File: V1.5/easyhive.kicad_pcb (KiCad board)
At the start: 2 copper layers, 35 x 75 mm, 104 parts, among them IC1 ATSAMD21G, IC2 BQ2407X, IC3 ADS1232, IC4 DS18B20U, IC5 XC6220B331, IC6 SARA-N310, IC7 TPS22919, J1 U.FL, J2 U.FL(2), K1 693043020611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

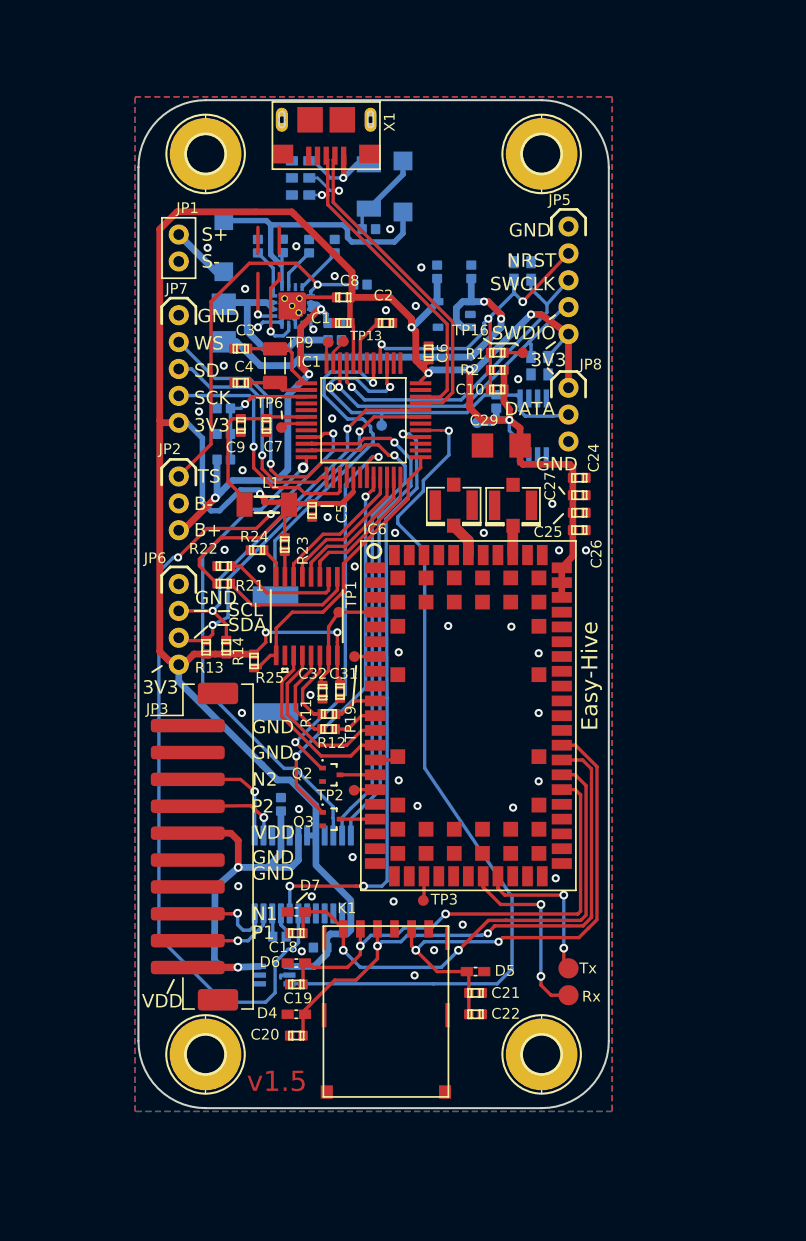
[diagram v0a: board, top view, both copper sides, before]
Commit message: v1.5 Oertel with optimizations
-fixed problems/questions from Oertel
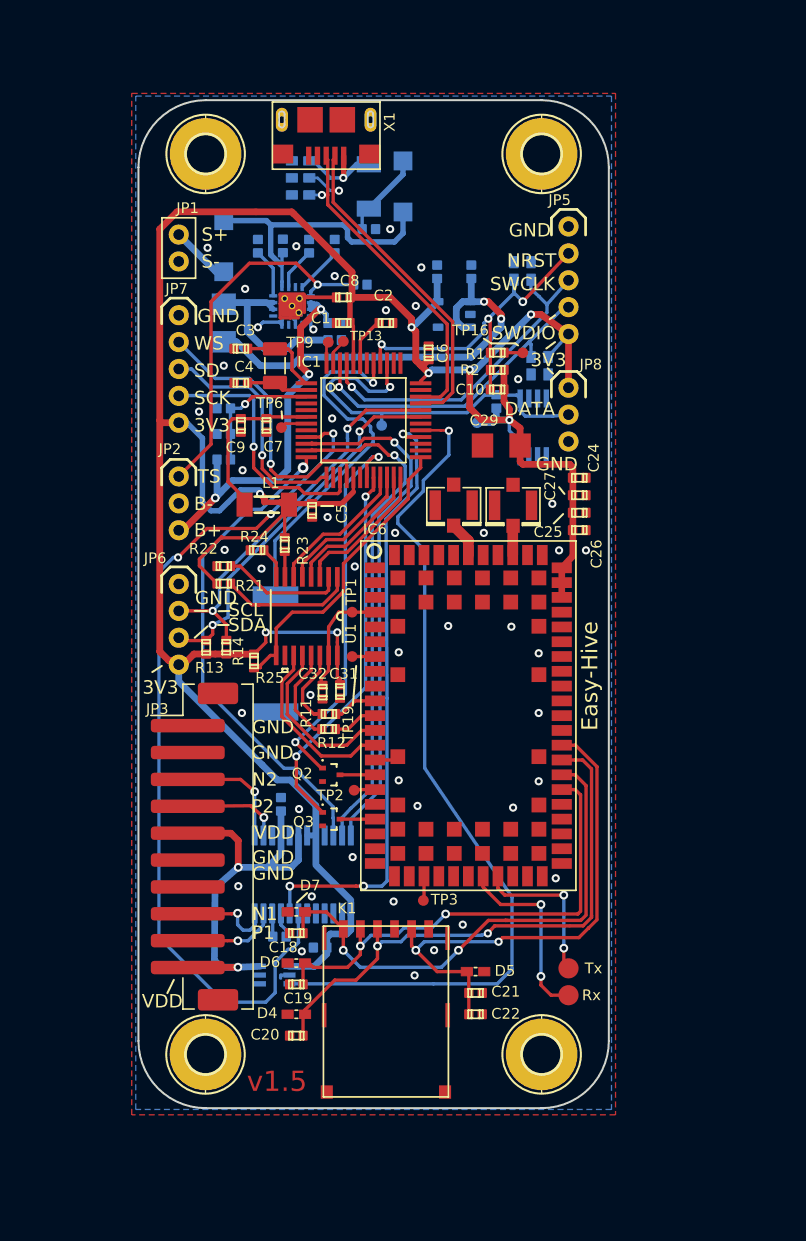
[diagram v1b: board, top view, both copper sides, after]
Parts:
- D1, D2: footprint easyhive:SOD123 -> easyhive:SOD-123
- L1, L2: value SM-1206 -> (none)
- moved TP1 1.00 mm to (146.9, 105.6)
- moved TP19 0.17 mm to (146.9, 108.9)
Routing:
- net Net-(IC2-Pad7): track 6.66 -> 0.00 mm, vias 1 -> 0
- net Net-(IC2-Pad9): track 4.25 -> 0.00 mm, vias 1 -> 0
- net Net-(LED2-PadA): track 1.92 -> 0.00 mm
- net Net-(LED1-PadA): track 1.92 -> 0.00 mm

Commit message: Begin Routing
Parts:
- removed IC6: SARA-N310, easyhive:SARA-N3
- removed J2: U.FL(2), easyhive:U.FL
- removed R11, R12, R21: 0R, easyhive:C0402
- removed TP1, TP19, TP2, TP3: TPTP08R, easyhive:TP08R
- added D15: PESD0402-140, easyhive:0402-TVS, F.Cu at (153.2, 102.3)
- added JP10: USB_BC66, easyhive:1X04-2MM_klein, F.Cu at (163.0, 127.8)
- added JP9: DBG, easyhive:1X02_2MM_klein, F.Cu at (163.0, 96.0)
- added Q4: DTC123JET1G, easyhive:SC75_SOT416, F.Cu at (156.4, 125.8)
- added R6: 10K, easyhive:C0402, F.Cu at (141.9, 122.7)
- added R7: 22R, easyhive:C0402, F.Cu at (144.5, 123.8)
- added R8: 22R, easyhive:C0402, F.Cu at (143.2, 123.8)
- added R9: 22R, easyhive:C0402, F.Cu at (145.8, 124.2)
- added U2: BC66, easyhive:Quectel_BC66, F.Cu at (155.2, 113.8)
- C22: value 100n -> 100nF
- D1, D2: footprint easyhive:SOD-123 -> easyhive:SOD123
- JP4: value M02-JST-2MM-SMT -> AUX; footprint easyhive:1X02_2MM_Pad_only -> easyhive:1X02_2MM_klein
- L1, L2: value (none) -> SM-1206
- moved C24 10.8 mm to (153.1, 97.0)
- moved C26 10.8 mm to (153.1, 100.9)
- moved C25 10.8 mm to (153.1, 99.6)
- moved C27 10.8 mm to (153.1, 98.3)
- moved JP4 9.10 mm to (163.0, 123.0)
- moved Q3 8.17 mm to (152.0, 125.8)
- moved J1 6.78 mm to (163.0, 103.0)
- moved C22 4.52 mm to (156.0, 131.0), turned to 270 degrees
- moved C31 2.12 mm to (144.5, 113.0)
- moved U1 2.12 mm to (142.5, 107.8)
- moved C32 2.05 mm to (143.2, 113.0)
- moved R23 1.88 mm to (140.8, 102.1)
- moved Q2 1.70 mm to (143.8, 116.9)
- moved C29 1.39 mm to (157.3, 94.4), turned to 0 degrees
- moved R25 1.30 mm to (138.8, 108.2), turned to 0 degrees
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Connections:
- net /SARA_1V8_ENABLE renamed /BC66_1V8_ENABLE
- net /SARA_CTS_3V3 renamed /BC66_RI_3V3
- net /SARA_PWRON renamed /BC66_PWRON
- net /SARA_RST renamed /BC66_RST
- net /SARA_RX_3V3 renamed /BC66_RXD_3V3
- net /SARA_TX_3V3 renamed /BC66_TXD_3V3
- C22 pad 1: Net-(C21-Pad1) -> GND
- C22 pad 2: GND -> Net-(C21-Pad1)
- IC1 pad 24: /SARA_RTS_3V3 -> Net-(IC1-Pad24)
- IC1 pad 8: Net-(IC1-Pad8) -> /BC66_PSM
- J1 pad P$3: /ANT -> Net-(J1-PadP$3)
- R23 pad 1: +3V3 -> GND
- R24 pad 1: GND -> +3V3
- U1 pad 11: /SARA_RX_1V8 -> /BC66_RXD_1V8
- U1 pad 12: /SARA_TX_1V8 -> /BC66_TXD_1V8
- U1 pad 13: /CTS1V8 -> /BC66_RI_1V8
- U1 pad 14: /RTS1V8 -> Net-(U1-Pad14)
- U1 pad 3: /SARA_RTS_3V3 -> Net-(U1-Pad3)
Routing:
- net Net-(C18-Pad1): track 38.8 -> 5.02 mm, vias 2 -> 0
- net Net-(C21-Pad1): track 38.5 -> 9.19 mm, vias 2 -> 0
- net Net-(C20-Pad1): track 41.6 -> 13.7 mm, vias 2 -> 1
- net Net-(C19-Pad1): track 35.9 -> 15.5 mm
- net +3V3: track 213.0 -> 194.5 mm, vias 8 -> 6
- net Net-(JP4-Pad2): track 14.0 -> 0.00 mm, vias 2 -> 0
- net /SARA_RX_1V8: track 13.4 -> 0.00 mm
- net /SARA_TX_1V8: track 12.8 -> 0.00 mm
- net /BC66_RST: track 28.5 -> 16.0 mm, vias 2 -> 1
- net Net-(JP9-Pad1): track 0.00 -> 12.0 mm
- net Net-(JP4-Pad1): track 11.6 -> 0.00 mm, vias 2 -> 0
- net /SARA_RTS_3V3: track 10.7 -> 0.00 mm
- net Net-(U1-Pad1): track 10.4 -> 0.00 mm
- net Net-(JP9-Pad2): track 0.00 -> 9.55 mm
- net /+1V8: track 8.65 -> 0.00 mm
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- removed copper zone on B.Cu, net GND
- removed copper zone on F.Cu, net GND

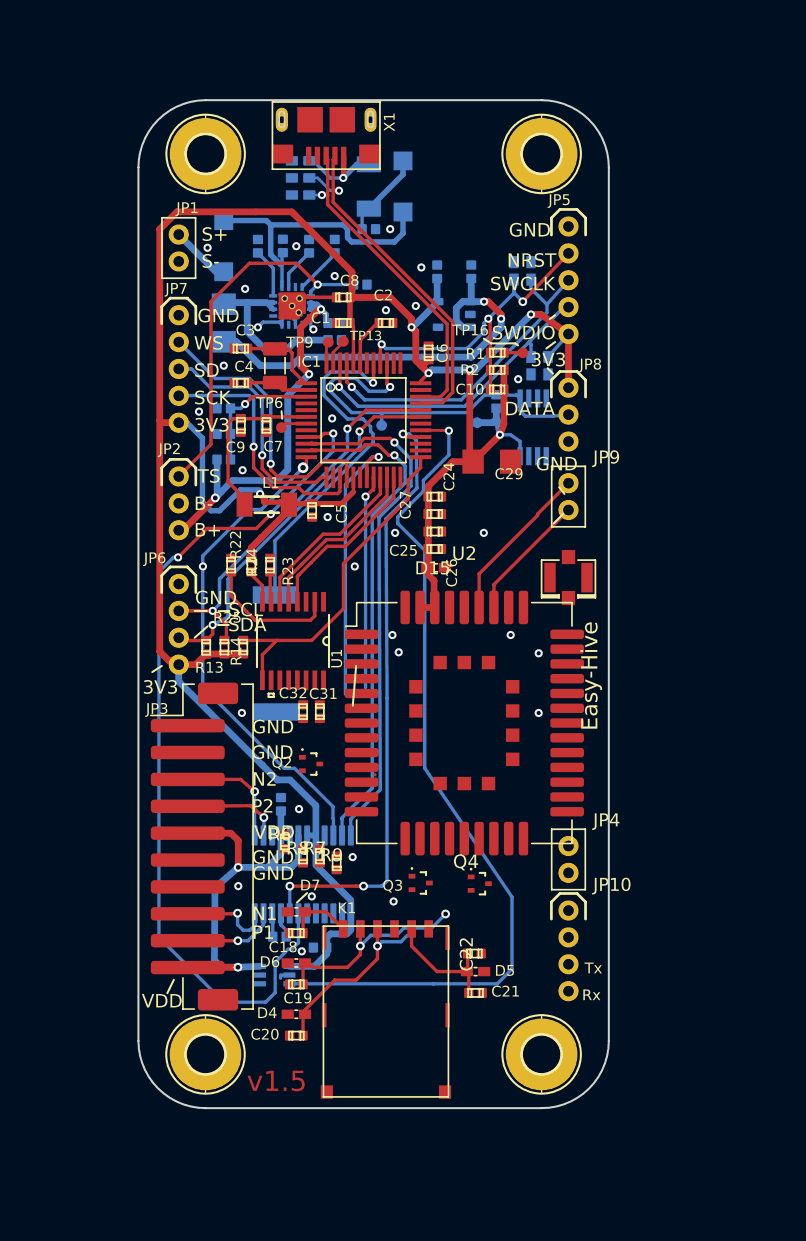
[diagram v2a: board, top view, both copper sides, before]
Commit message: try to route...
DRC Checker meckert wegen Bauteilüberschneidung. BC66 hat im Footprint mega Rahmen... Laut Description ist es 17,7mm breit, der Rahmen hat aber über 20mm...
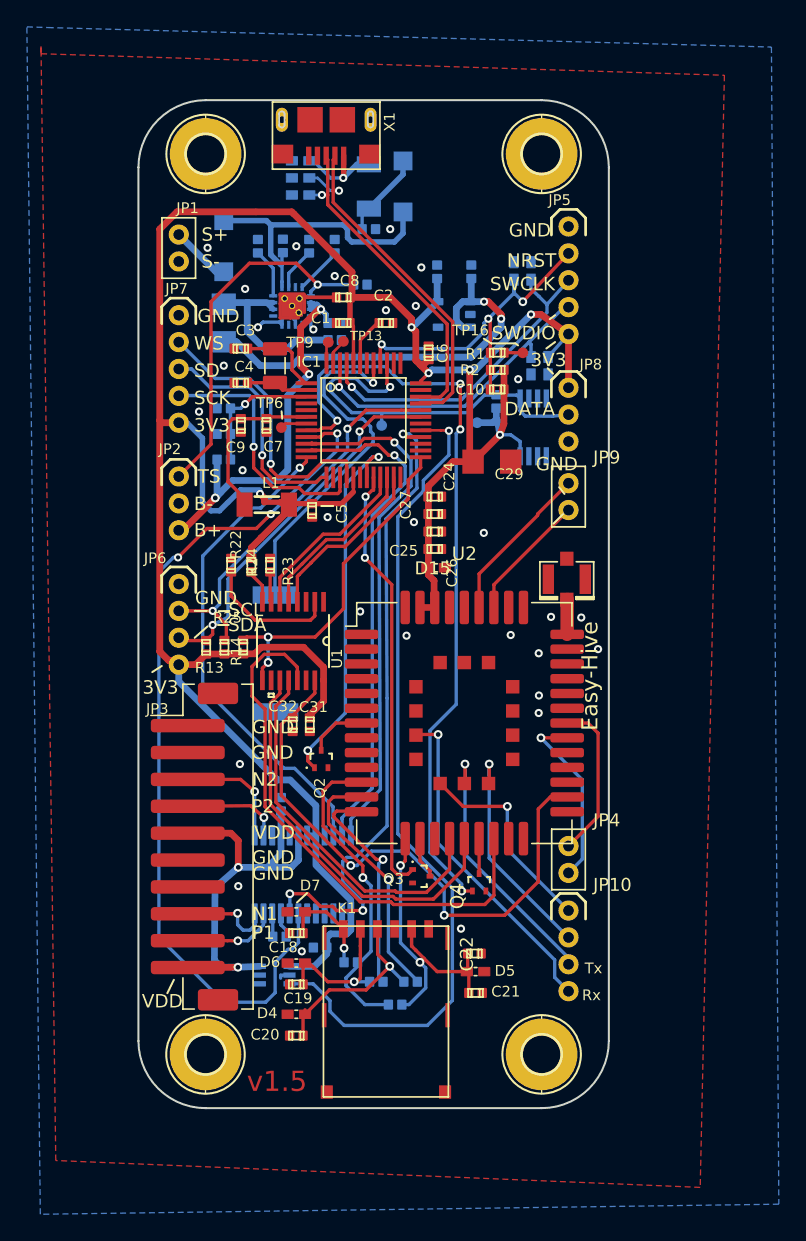
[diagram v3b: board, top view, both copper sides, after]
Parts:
- R6, R7, R8, R9: moved to B.Cu
- moved R6 14.6 mm to (150.1, 134.8), turned to 90 degrees
- moved R7 11.5 mm to (151.2, 133.1), turned to 90 degrees
- moved R9 9.33 mm to (148.7, 133.1), turned to 90 degrees
- moved R8 8.66 mm to (146.8, 131.7), turned to 90 degrees
- moved C32 1.25 mm to (142.5, 114.0)
- moved C31 1.23 mm to (143.8, 114.0)
- moved Q2 0.84 mm to (144.6, 116.5), turned to 90 degrees
- moved Q3 0.50 mm to (152.0, 125.2)
- moved J1 0.18 mm to (162.9, 103.2)
- moved Q4 0.11 mm to (156.3, 125.7), turned to 90 degrees
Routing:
- net /BC66_PSM: track 0.00 -> 58.4 mm, vias 0 -> 4
- net /+1V8: track 0.00 -> 44.1 mm, vias 0 -> 2
- net /BC66_RI_1V8: track 0.00 -> 40.5 mm
- net /BC66_RXD_1V8: track 0.00 -> 30.0 mm
- net /BC66_TXD_1V8: track 0.00 -> 28.2 mm
- net Net-(JP10-Pad4): track 0.00 -> 24.8 mm, vias 0 -> 1
- net Net-(R6-Pad2): track 0.00 -> 23.7 mm, vias 0 -> 1
- net Net-(JP10-Pad3): track 0.00 -> 19.6 mm, vias 0 -> 1
- net Net-(R7-Pad1): track 0.00 -> 18.8 mm, vias 0 -> 1
- net Net-(R9-Pad1): track 0.00 -> 17.0 mm, vias 0 -> 1
- net Net-(JP10-Pad2): track 0.00 -> 16.8 mm, vias 0 -> 1
- net /BC66_RST: track 16.0 -> 32.2 mm, vias 1 -> 2
- net Net-(JP10-Pad1): track 0.00 -> 15.3 mm, vias 0 -> 1
- net Net-(C21-Pad1): track 9.19 -> 23.9 mm, vias 0 -> 2
- net Net-(JP4-Pad2): track 0.00 -> 13.7 mm, vias 0 -> 1
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- added copper zone on B.Cu, net GND
- added copper zone on F.Cu, net GND

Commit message: Routing done. Need double check and move Silk
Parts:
- moved Q3 24.4 mm to (149.6, 101.0)
- moved JP9 6.93 mm to (156.4, 98.2), turned to 0 degrees
- moved R14 4.21 mm to (136.7, 104.0), turned to 90 degrees
- moved J1 3.63 mm to (162.7, 99.5)
- moved R25 2.51 mm to (136.4, 109.0)
- moved JP4 2.24 mm to (164.0, 125.0), turned to 180 degrees
- moved R13 2.23 mm to (136.8, 106.1), turned to 90 degrees
- moved C31 2.20 mm to (143.4, 111.8)
- moved U1 1.96 mm to (141.2, 106.3)
- moved Q2 1.52 mm to (143.1, 116.8)
- moved R23 1.36 mm to (140.0, 101.0)
- moved R24 1.36 mm to (138.6, 101.0)
- moved R22 1.30 mm to (137.2, 101.0)
- moved Q4 1.05 mm to (156.3, 126.8)
- moved JP10 0.70 mm to (163.0, 128.5)
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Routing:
- net /BC66_RST: track 32.2 -> 8.37 mm
- net Net-(Q3-Pad3): track 3.11 -> 23.8 mm
- net +3V3: track 205.5 -> 210.8 mm
- net /BC66_RI_1V8: track 40.5 -> 45.4 mm
- net Net-(JP9-Pad1): track 12.0 -> 7.14 mm
- net /SAM_SCL: track 28.9 -> 25.2 mm
- net Net-(J1-PadP$3): track 2.74 -> 6.20 mm
- net Net-(R9-Pad1): track 17.0 -> 14.0 mm
- net Net-(JP10-Pad3): track 19.6 -> 16.8 mm
- net Net-(JP10-Pad2): track 16.8 -> 14.1 mm
- net /BC66_PSM: track 58.4 -> 60.9 mm
- net Net-(JP9-Pad2): track 9.55 -> 7.52 mm
- net /BC66_1V8_ENABLE: track 25.7 -> 27.7 mm
- net /+1V8: track 44.1 -> 46.1 mm
- net /BC66_PWRON: track 28.2 -> 30.0 mm
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
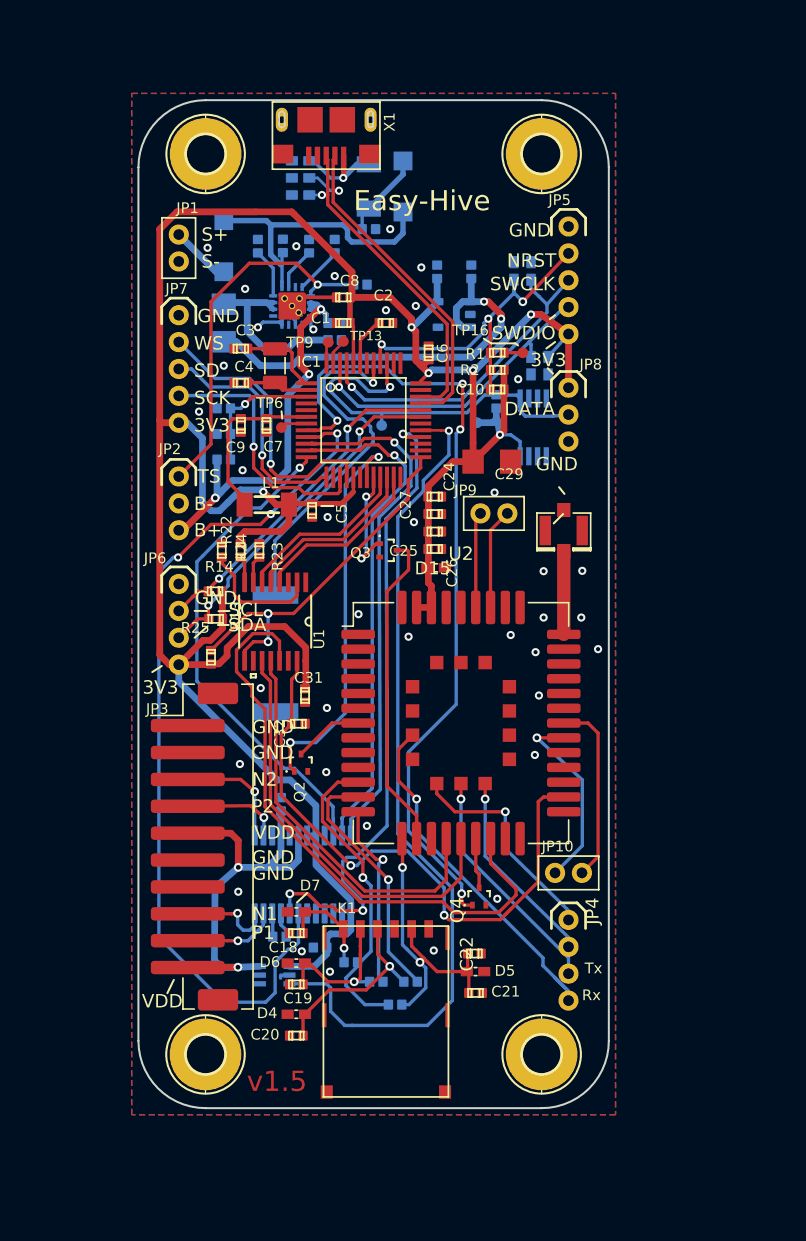
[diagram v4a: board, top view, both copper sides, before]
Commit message: Need verification.
-Routing done
-Silk done
-USB Mode 2 drill Pads + R10k
-open review
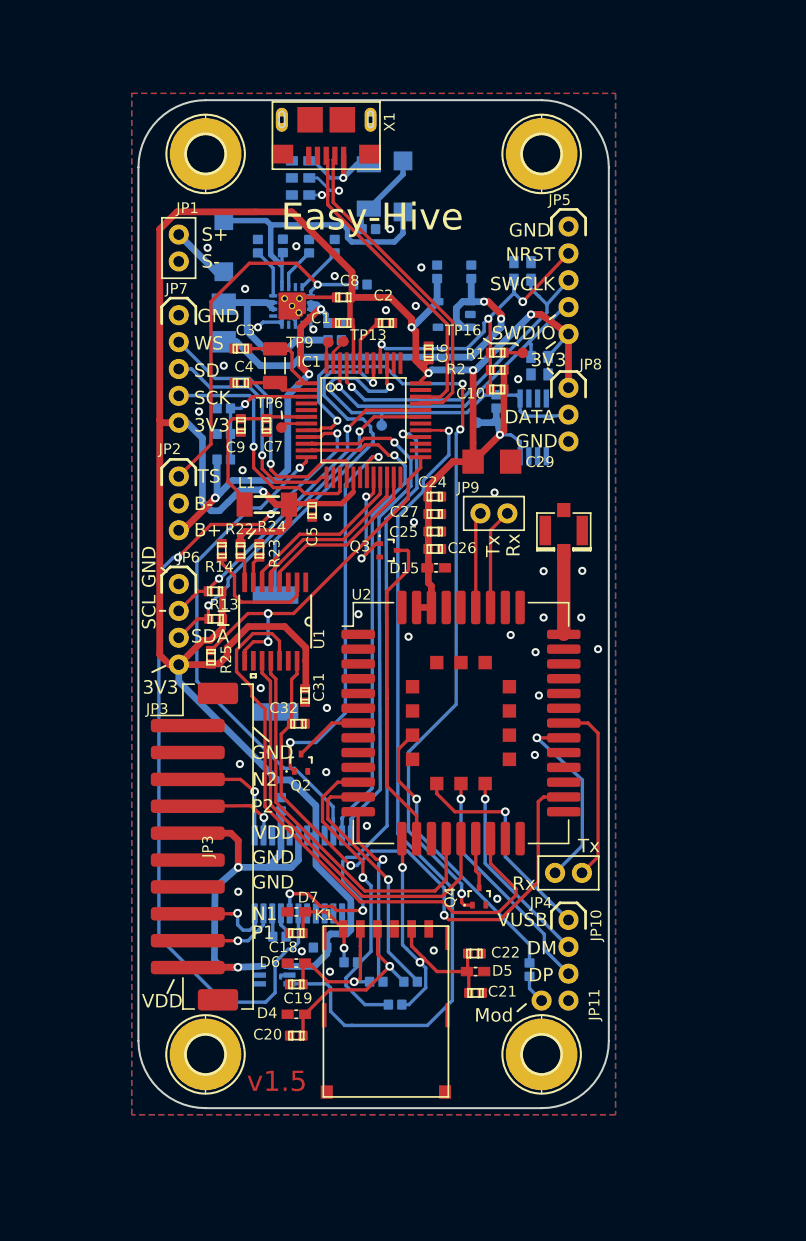
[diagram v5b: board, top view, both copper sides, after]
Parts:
- added JP11: USB_MODE, easyhive:1X02_2MM_klein, F.Cu at (161.0, 134.5)
- added R10: 10K, easyhive:C0402, B.Cu at (160.1, 132.2)
- JP10: footprint easyhive:1X04-2MM_klein -> easyhive:1X03-2MM_klein
- JP4: value AUX -> UART_AUX
- JP9: value DBG -> UART_DBG
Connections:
- U2 pad 47: Net-(JP10-Pad4) -> Net-(R10-Pad1)
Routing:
- net Net-(JP10-Pad4): track 26.2 -> 0.00 mm, vias 1 -> 0
- net Net-(R10-Pad1): track 0.00 -> 21.3 mm, vias 0 -> 1
- net Net-(JP11-Pad1): track 0.00 -> 2.17 mm
- net Net-(JP10-Pad3): track 16.8 -> 17.5 mm
- net Net-(JP10-Pad1): track 15.7 -> 16.4 mm
- net Net-(JP10-Pad2): track 14.1 -> 14.7 mm
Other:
- board text added: "DM"
- board text added: "DP"
- board text added: "Mod"
- board text added: "VUSB"
